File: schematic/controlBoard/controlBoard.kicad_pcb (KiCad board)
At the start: 2 copper layers, 55 x 55 mm, 40 parts, among them CON0 PINHD-1X10, IC2 DS3231/SO, IC3 LM1117?-MP, IC4 ESP12ESMD, T1 BC547, T2 BC547, Y1 12MHz

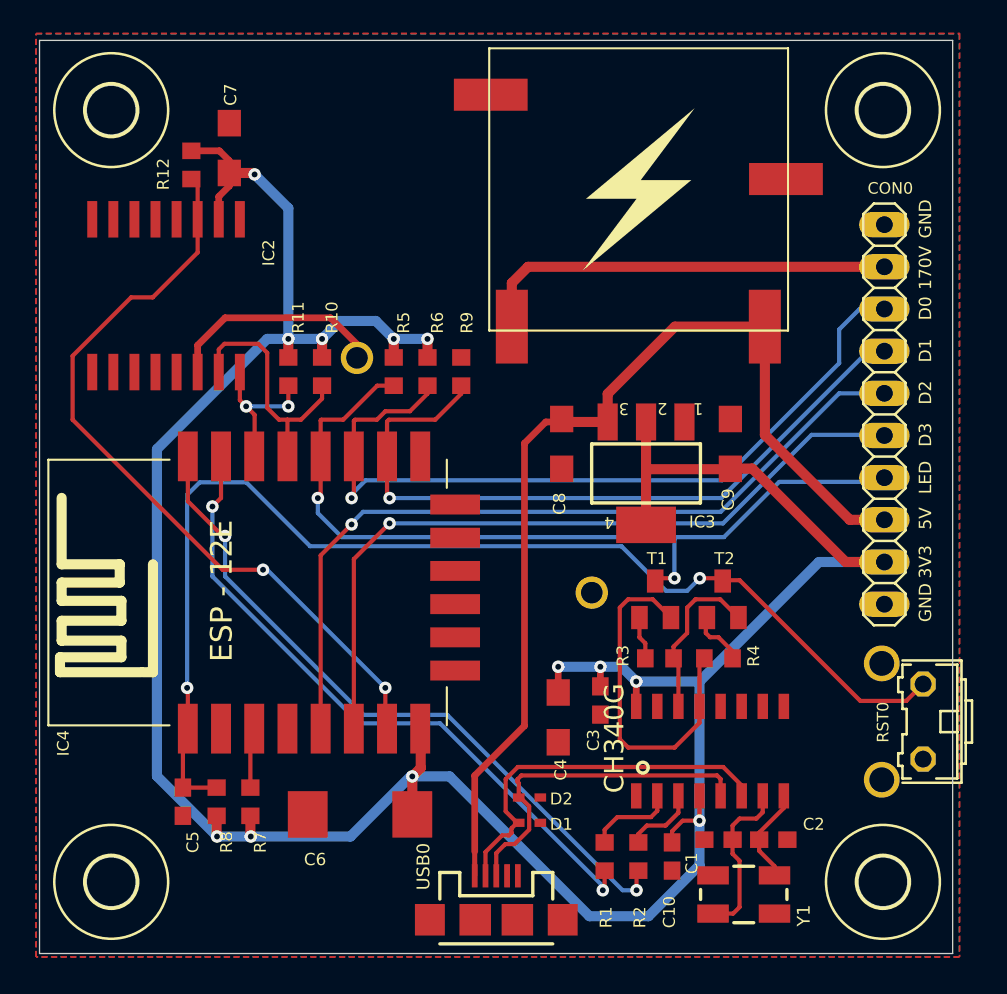
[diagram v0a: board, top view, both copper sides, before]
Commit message: Use usb type C connector and re-wire control board with KiCad components
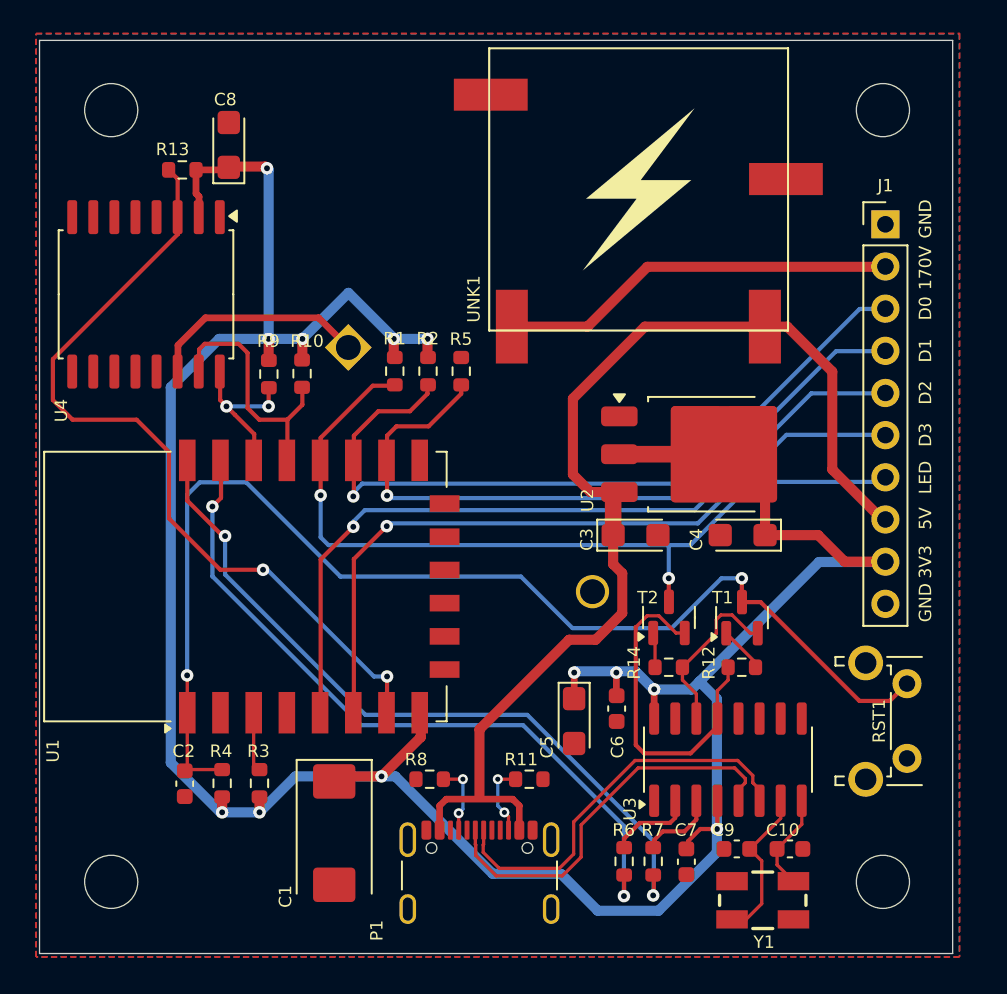
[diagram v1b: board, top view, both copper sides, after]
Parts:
- removed CON0: PINHD-1X10, controlBoard:1X10_325
- removed D1, D2: ESD321, controlBoard:SOD523_210
- removed IC2: DS3231/SO, controlBoard:SO16W
- removed IC3: LM1117?-MP, controlBoard:SOT223
- removed IC4: ESP12ESMD, controlBoard:ESP12E-SMD
- removed RST0: 31-XX, controlBoard:B3F-31XX_377
- removed U$2: CH340G, controlBoard:SOIC16
- removed USB0: USB_MICRO-B_SMT, controlBoard:USB-MICROB_513
- added J1: Conn_01x10_Pin, Connector_PinHeader_2.54mm:PinHeader_1x10_P2.54mm_Vertical, F.Cu at (171.9, 88.6)
- added P1: USB_C_Plug_USB2.0, Connector_USB:USB_C_Receptacle_GCT_USB4105-xx-A_16P_TopMnt_Horizontal, F.Cu at (147.5, 128.8)
- added R13: 4k7, Resistor_SMD:R_0603_1608Metric, F.Cu at (129.6, 85.3)
- added R14: 12k, Resistor_SMD:R_0603_1608Metric, F.Cu at (158.9, 115.3)
- added RST1: SW_Push, Button_Switch_THT:SW_Tactile_SPST_Angled_PTS645Vx31-2LFS, F.Cu at (173.3, 116.2)
- added U1: ESP-12E, RF_Module:ESP-12E, F.Cu at (133.4, 110.4)
- added U2: LM1117DT-3.3, Package_TO_SOT_SMD:TO-252-3_TabPin2, F.Cu at (161.0, 102.4)
- added U3: CH340G, Package_SO:SOIC-16_3.9x9.9mm_P1.27mm, F.Cu at (162.5, 120.8)
- added U4: DS3231M, Package_SO:SOIC-16W_7.5x10.3mm_P1.27mm, F.Cu at (127.4, 92.8)
- BT1: value BATTERY-20MM_PTH -> Battery_Cell; footprint controlBoard:BATTCOM_20MM_PTH -> Battery:BatteryHolder_MYOUNG_BS-07-A1BJ001_CR2032
- C1: value 22p -> 100u/16V; footprint controlBoard:C0603_348 -> Capacitor_Tantalum_SMD:CP_EIA-7343-31_Kemet-D
- C10: value 100n -> 22p; footprint controlBoard:C0603_348 -> Capacitor_SMD:C_0603_1608Metric
- C2: value 22p -> 470p; footprint controlBoard:C0603_348 -> Capacitor_SMD:C_0603_1608Metric
- C3: value 100n -> 10u; footprint controlBoard:C0603_348 -> Capacitor_Tantalum_SMD:CP_EIA-3216-10_Kemet-I
- C4: footprint controlBoard:SMC_A_348 -> Capacitor_Tantalum_SMD:CP_EIA-3216-10_Kemet-I
- C5: value 470p -> 10u; footprint controlBoard:C0603_348 -> Capacitor_Tantalum_SMD:CP_EIA-3216-10_Kemet-I
- C6: value 100u/16V -> 100n; footprint controlBoard:SMC_D_348 -> Capacitor_SMD:C_0603_1608Metric
- C7: value 1u -> 100n; footprint controlBoard:SMC_A_348 -> Capacitor_SMD:C_0603_1608Metric
- C8: value 10u -> 1u; footprint controlBoard:SMC_A_348 -> Capacitor_Tantalum_SMD:CP_EIA-3216-10_Kemet-I
- C9: value 10u -> 22p; footprint controlBoard:SMC_A_348 -> Capacitor_SMD:C_0603_1608Metric
- H1, H2, H3, H4: value MOUNT-HOLE3.0 -> MountingHole; footprint controlBoard:3,0_237 -> MountingHole:MountingHole_3.2mm_M3
- R1, R2: value 470 -> 12k; footprint controlBoard:R0603_348 -> Resistor_SMD:R_0603_1608Metric
- R10, R3, R4, R5: footprint controlBoard:R0603_348 -> Resistor_SMD:R_0603_1608Metric
- R11: value 4k7 -> 5k1; footprint controlBoard:R0603_348 -> Resistor_SMD:R_0603_1608Metric
- R12: value 4k7 -> 12k; footprint controlBoard:R0603_348 -> Resistor_SMD:R_0603_1608Metric
- R6, R7: value 12k -> 470; footprint controlBoard:R0603_348 -> Resistor_SMD:R_0603_1608Metric
- R8: value 12k -> 5k1; footprint controlBoard:R0603_348 -> Resistor_SMD:R_0603_1608Metric
- R9: value 12k -> 4k7; footprint controlBoard:R0603_348 -> Resistor_SMD:R_0603_1608Metric
- T1, T2: value BC547 -> BC847; footprint controlBoard:SOT23-BEC_402 -> Package_TO_SOT_SMD:SOT-23
- moved C7 51.0 mm to (160.0, 127.0)
- moved R12 44.9 mm to (163.3, 115.3), turned to 0 degrees
- moved C2 35.6 mm to (129.8, 122.3), turned to -90 degrees
- moved R2 31.9 mm to (144.4, 97.4), turned to 90 degrees
- moved R1 31.9 mm to (142.4, 97.4), turned to 90 degrees
- moved R6 31.8 mm to (156.2, 127.0), turned to -90 degrees
- moved R4 30.8 mm to (132.0, 122.2), turned to -90 degrees
- moved R11 28.5 mm to (150.5, 122.0), turned to 0 degrees
- moved C8 27.0 mm to (132.4, 83.8), turned to 90 degrees
- moved R3 25.2 mm to (134.2, 122.2), turned to -90 degrees
- moved R7 24.5 mm to (158.0, 127.0)
- moved C9 24.4 mm to (163.0, 126.2), turned to 180 degrees
- moved C5 24.1 mm to (153.2, 118.5)
- moved C1 23.1 mm to (138.8, 125.2), turned to -90 degrees
- moved C6 16.7 mm to (155.8, 117.8), turned to -90 degrees
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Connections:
- C1 pad 1: GND -> +3V3
- C1 pad 2: /XI -> GND
- C10 pad 1: +3V3 -> Net-(U3-XO)
- C2 pad 1: GND -> /RST
- C2 pad 2: /XO -> GND
- C3 pad 1: GND -> +5V
- C3 pad 2: +3V3 -> GND
- C5 pad 1: /RST -> +3V3
- R1 pad 1: Net-(U$2-TX) -> /GPIO0
- R1 pad 2: /RX -> +3V3
- R10 pad 1: +3V3 -> /SDA
- R10 pad 2: /SDA -> +3V3
- R11 pad 1: +3V3 -> Net-(P1-VCONN)
- R11 pad 2: /SCL -> GND
- R12 pad 1: +3V3 -> Net-(T2-E)
- R12 pad 2: /SQW -> Net-(T1-B)
- R2 pad 1: Net-(U$2-RX) -> /GPIO2
- R2 pad 2: /TX -> +3V3
- R3 pad 1: Net-(R3-Pad1) -> /EN
- R3 pad 2: Net-(U$2-RTS) -> +3V3
- R4 pad 1: Net-(R4-Pad1) -> /RST
- R4 pad 2: Net-(U$2-DTR) -> +3V3
- R5 pad 1: /GPIO0 -> /GPIO15
- R5 pad 2: +3V3 -> GND
- R6 pad 1: /GPIO2 -> Net-(U3-TXD)
- R6 pad 2: +3V3 -> /RX
- R7 pad 1: /EN -> Net-(U3-RXD)
- R7 pad 2: +3V3 -> /TX
- R8 pad 1: /RST -> Net-(P1-CC)
- R8 pad 2: +3V3 -> GND
- R9 pad 1: /GPIO15 -> /SCL
- R9 pad 2: GND -> +3V3
- UNK1 pad OUT: 170V -> VCC
- Y1 pad 1: /XI -> Net-(U3-XI)
- Y1 pad 3: /XO -> Net-(U3-XO)
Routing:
- net 170V: track 25.5 -> 0.00 mm
- net /D-: track 0.00 -> 24.5 mm
- net VCC: track 0.00 -> 23.9 mm
- net /D+: track 0.00 -> 23.9 mm
- net /D_N: track 22.8 -> 0.00 mm
- net Net-(U$2-DTR): track 21.3 -> 0.00 mm
- net /D_P: track 20.7 -> 0.00 mm
- net Net-(T2-E): track 0.00 -> 19.7 mm
- net Net-(T1-E): track 0.00 -> 10.2 mm
- net Net-(U$2-RTS): track 10.2 -> 0.00 mm
- net /XI: track 9.98 -> 0.00 mm
- net Net-(U3-XI): track 0.00 -> 9.47 mm
- net Net-(U3-XO): track 0.00 -> 6.61 mm
- net +5V: track 61.8 -> 68.0 mm
- net /XO: track 5.79 -> 0.00 mm
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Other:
- board text added: "Single digit nixie clock - Control board Daniel Knežević 2025"
- board text removed: "Single digit nixie clock - Control board Daniel Knežević 2024"

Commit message: Re-wire control display with KiCad components
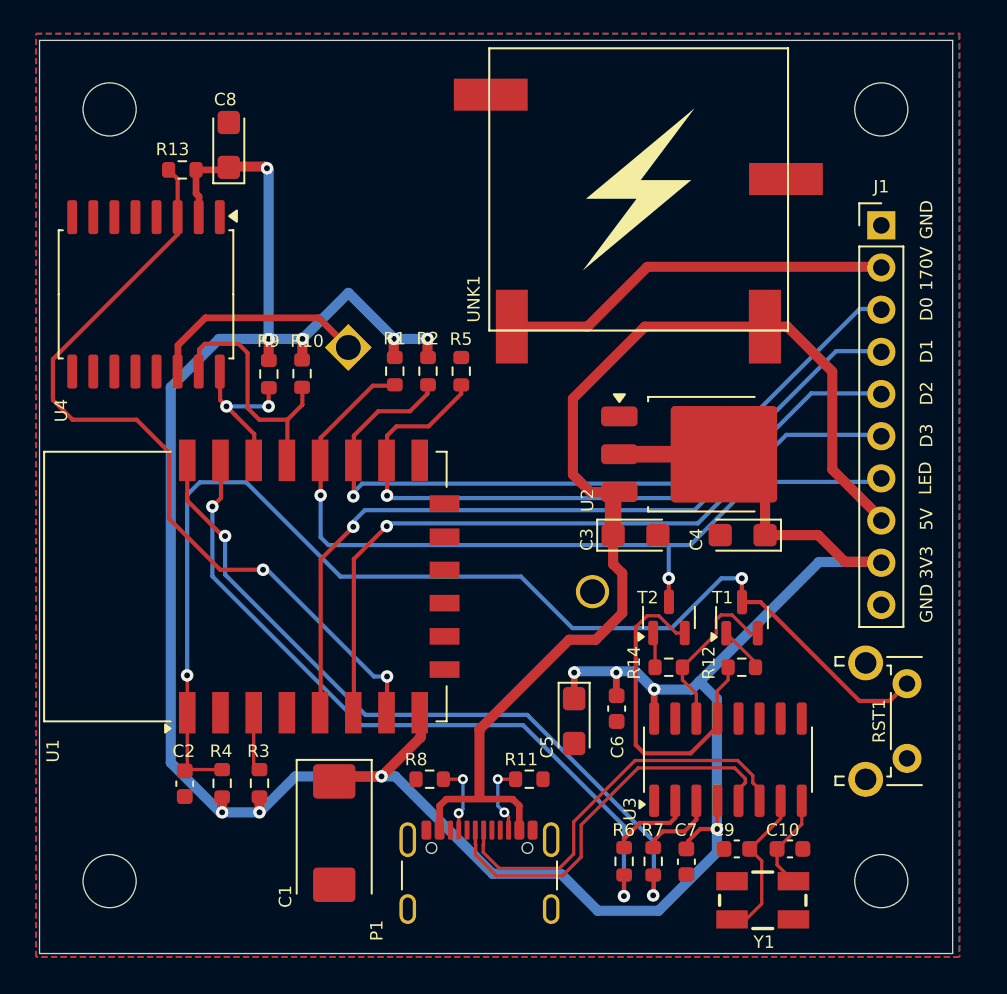
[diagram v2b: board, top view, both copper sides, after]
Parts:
- moved J1 0.25 mm to (171.7, 88.6)
- moved H2 0.11 mm to (125.2, 81.7)
- moved H3 0.11 mm to (125.2, 128.1)
- moved H1 0.11 mm to (171.7, 81.7)
- moved H4 0.11 mm to (171.7, 128.1)
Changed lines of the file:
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@@
 	(footprint "MountingHole:MountingHole_3.2mm_M3"
 		(layer "F.Cu")
-		(at 171.8011 81.7036)
+		(at 171.704 81.661)
 		(descr "Mounting Hole 3.2mm, no annular, M3")
 		(tags "mounting hole 3.2mm no annular m3")
@@
 	(footprint "MountingHole:MountingHole_3.2mm_M3"
 		(layer "F.Cu")
-		(at 125.3191 128.1856)
+		(at 125.222 128.143)
 		(descr "Mounting Hole 3.2mm, no annular, M3")
 		(tags "mounting hole 3.2mm no annular m3")
@@
 	(footprint "Connector_PinHeader_2.54mm:PinHeader_1x10_P2.54mm_Vertical"
 		(layer "F.Cu")
-		(at 171.95 88.58)
+		(at 171.704 88.646)
 		(descr "Through hole straight pin header, 1x10, 2.54mm pitch, single row")
 		(tags "Through hole pin header THT 1x10 2.54mm single row")
@@
 	(footprint "MountingHole:MountingHole_3.2mm_M3"
 		(layer "F.Cu")
-		(at 125.3191 81.7036)
+		(at 125.222 81.661)
 		(descr "Mounting Hole 3.2mm, no annular, M3")
 		(tags "mounting hole 3.2mm no annular m3")
@@
 	(footprint "MountingHole:MountingHole_3.2mm_M3"
 		(layer "F.Cu")
-		(at 171.8011 128.1856)
+		(at 171.704 128.143)
 		(descr "Mounting Hole 3.2mm, no annular, M3")
 		(tags "mounting hole 3.2mm no annular m3")
@@
 	)
 	(gr_text "170V"
-		(at 173.9211 89.8716 90)
+		(at 173.99 89.916 90)
 		(layer "F.SilkS")
 		(effects
@@
 	)
 	(gr_text "3V3"
-		(at 173.9211 107.9056 90)
+		(at 173.99 107.95 90)
 		(layer "F.SilkS")
 		(effects
@@
 	)
 	(gr_text "LED"
-		(at 173.9211 102.8256 90)
+		(at 173.9211 102.87 90)
 		(layer "F.SilkS")
 		(effects
@@
 	)
 	(gr_text "5V"
-		(at 173.9211 105.6196 90)
+		(at 173.99 105.664 90)
 		(layer "F.SilkS")
 		(effects
@@
 	)
 	(gr_text "D3"
-		(at 173.9211 100.5396 90)
+		(at 173.99 100.584 90)
 		(layer "F.SilkS")
 		(effects
@@
 	)
 	(gr_text "GND"
-		(at 173.9211 87.0776 90)
+		(at 173.99 87.122 90)
 		(layer "F.SilkS")
 		(effects
@@
 	)
 	(gr_text "D2"
-		(at 173.9211 97.9996 90)
+		(at 173.99 98.044 90)
 		(layer "F.SilkS")
 		(effects
@@
 	)
 	(gr_text "D1"
-		(at 173.9211 95.4596 90)
+		(at 173.99 95.504 90)
 		(layer "F.SilkS")
 		(effects
@@
 	)
 	(gr_text "D0"
-		(at 173.9211 92.9196 90)
+		(at 173.99 92.964 90)
 		(layer "F.SilkS")
 		(effects
@@
 	)
 	(gr_text "GND"
-		(at 173.9211 110.1916 90)
+		(at 173.99 110.236 90)
 		(layer "F.SilkS")
 		(effects

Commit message: Update control board with updated usb-c wiring
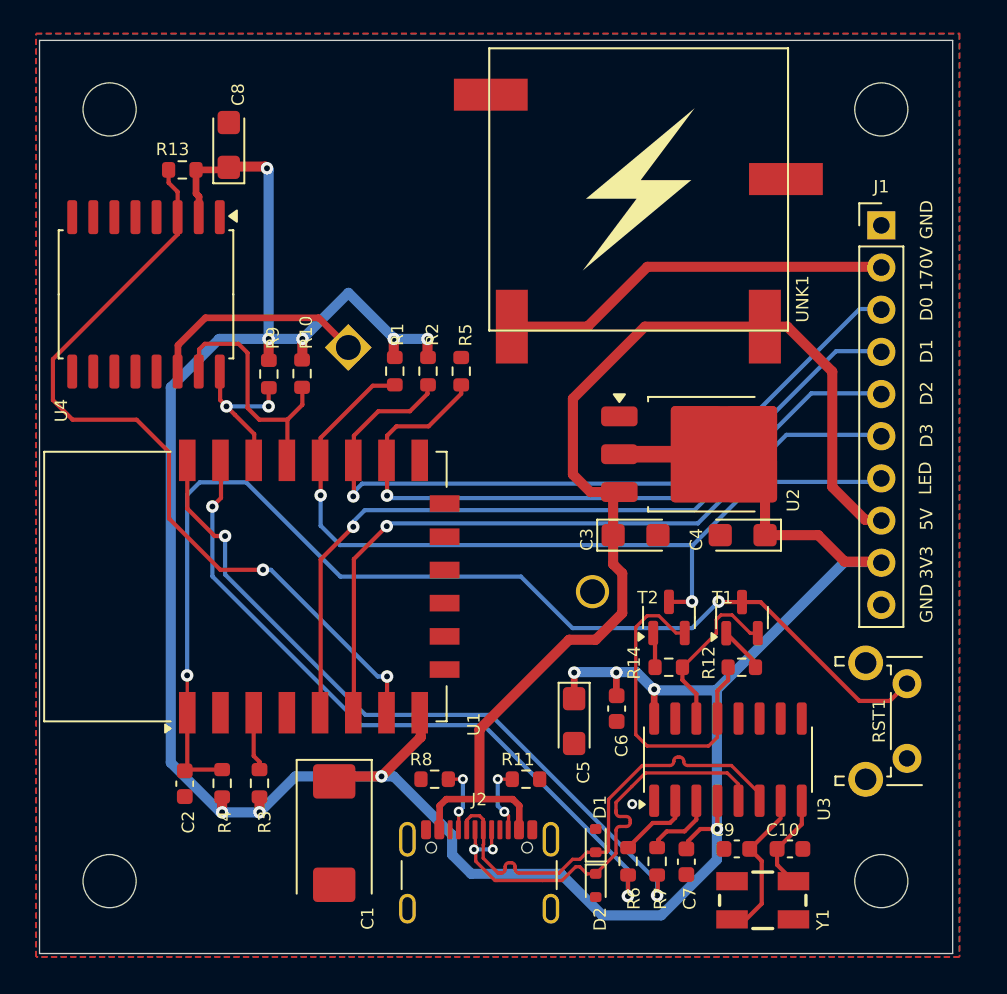
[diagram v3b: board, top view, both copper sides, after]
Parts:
- removed P1: USB_C_Plug_USB2.0, Connector_USB:USB_C_Receptacle_GCT_USB4105-xx-A_16P_TopMnt_Horizontal
- added D1: ESD321, Diode_SMD:D_SOD-523, F.Cu at (154.5, 125.7)
- added D2: ESD321, Diode_SMD:D_SOD-523, F.Cu at (154.5, 128.4)
- added J2: USB_C_Receptacle_USB2.0_14P, Connector_USB:USB_C_Receptacle_GCT_USB4105-xx-A_16P_TopMnt_Horizontal, F.Cu at (147.5, 128.7)
- moved R8 0.30 mm to (144.8, 122.0)
- moved R6 0.24 mm to (156.5, 127.0)
- moved R7 0.24 mm to (158.2, 127.0)
- moved R11 0.20 mm to (150.3, 122.0)
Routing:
- net /D+: track 23.9 -> 27.9 mm, vias 0 -> 2
- net /D-: track 24.5 -> 28.1 mm
- net /RX: track 43.6 -> 42.4 mm
- net /RST: track 71.1 -> 69.9 mm
- net /GPIO0: track 51.2 -> 52.1 mm
- net /TX: track 45.1 -> 44.2 mm
- net +5V: track 68.0 -> 68.6 mm
- net Net-(U3-TXD): track 4.99 -> 4.44 mm
- net GND: vias 0 -> 1

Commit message: Use ESP32 instead of ESP8266
- Re-route PCB to support ESP32
- Fill top plane with +3v3
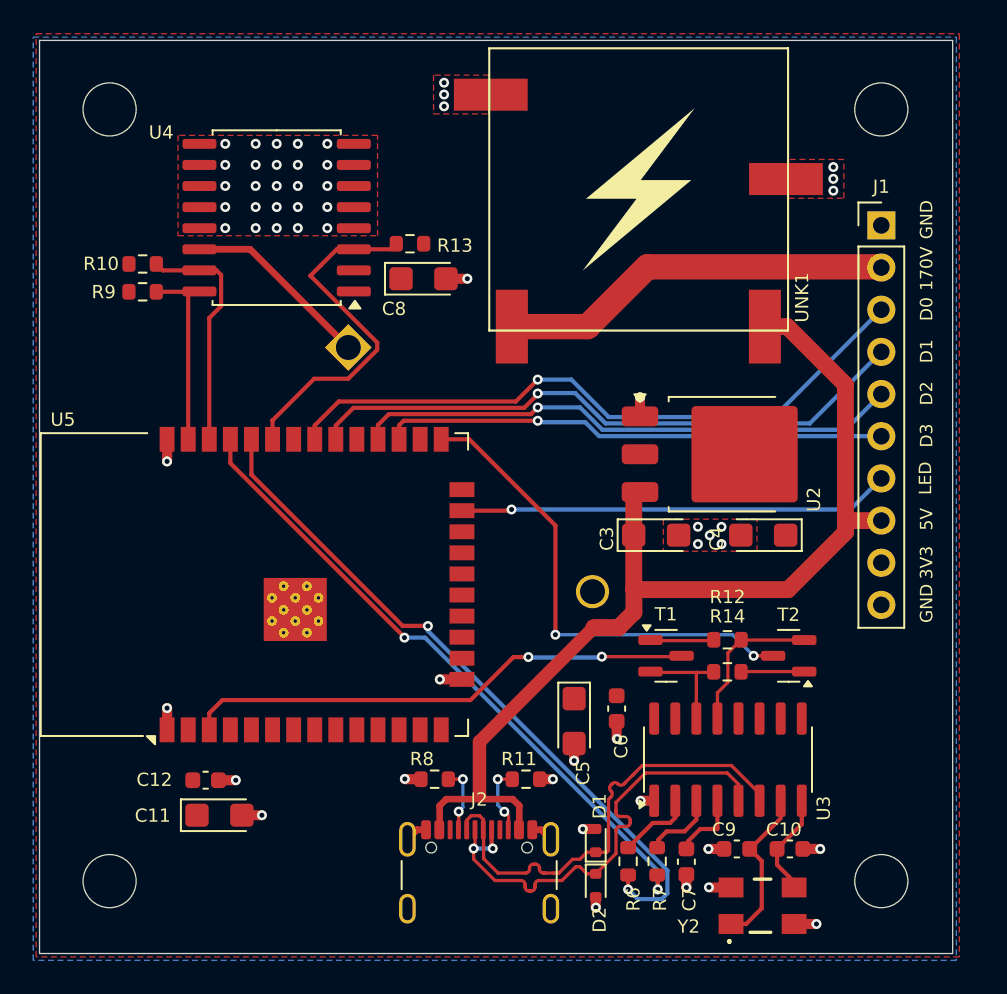
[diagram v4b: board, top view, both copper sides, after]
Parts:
- removed C1: 100u/16V, Capacitor_Tantalum_SMD:CP_EIA-7343-31_Kemet-D
- removed C2: 470p, Capacitor_SMD:C_0603_1608Metric
- removed R1, R2, R3, R4, R5: 12k, Resistor_SMD:R_0603_1608Metric
- removed RST1: SW_Push, Button_Switch_THT:SW_Tactile_SPST_Angled_PTS645Vx31-2LFS
- removed U1: ESP-12E, RF_Module:ESP-12E
- removed Y1: 12MHz, controlBoard:CRYSTAL-SMD-5X3.2-4PAD
- added C11: 10u, Capacitor_Tantalum_SMD:CP_EIA-3216-10_Kemet-I, F.Cu at (131.8, 124.2)
- added C12: 100n, Capacitor_SMD:C_0603_1608Metric, F.Cu at (131.0, 122.1)
- added U5: ESP32-WROOM-32D, RF_Module:ESP32-WROOM-32D-no-keepout, F.Cu at (136.9, 110.3)
- added Y2: 405I35D25M00000, cristal:405I35D25M00000, F.Cu at (164.6, 129.6)
- moved R13 14.4 mm to (143.3, 89.8)
- moved C8 14.2 mm to (144.1, 91.9), turned to 0 degrees
- moved R10 11.7 mm to (127.2, 91.0), turned to 180 degrees
- moved U4 9.12 mm to (135.3, 88.2), turned to 180 degrees
- moved R9 9.07 mm to (127.2, 92.6), turned to 180 degrees
- moved T2 7.57 mm to (166.1, 114.6), turned to 180 degrees
- moved T1 5.12 mm to (158.7, 114.6), turned to 0 degrees
- moved R14 3.54 mm to (162.4, 115.5), turned to 0 degrees
- moved R12 1.87 mm to (162.4, 113.6), turned to 180 degrees
- moved C4 1.24 mm to (164.6, 107.3)
- moved C3 1.24 mm to (158.1, 107.3)
- moved U2 1.24 mm to (162.2, 102.4)
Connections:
- net Net-(U3-XI) renamed /XI
- net Net-(U3-XO) renamed /XO
- J1 pad 3: /GPIO2 -> /D0
- J1 pad 4: /GPIO15 -> /D1
- J1 pad 5: /GPIO14 -> /D2
- J1 pad 6: /GPIO12 -> /D3
- J1 pad 7: /GPIO0 -> /RGBLED
- T1 pad 3: /RST -> /EN
- T2 pad 3: /GPIO0 -> /IO0
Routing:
- net +3V3: track 171.8 -> 5.14 mm, vias 12 -> 0
- net /RST: track 69.9 -> 0.00 mm, vias 2 -> 0
- net /GPIO0: track 52.1 -> 0.00 mm, vias 2 -> 0
- net /GPIO14: track 48.5 -> 0.00 mm, vias 1 -> 0
- net /GPIO2: track 46.4 -> 0.00 mm, vias 1 -> 0
- net /GPIO12: track 45.3 -> 0.00 mm, vias 1 -> 0
- net /GPIO15: track 43.3 -> 0.00 mm, vias 1 -> 0
- net /D0: track 0.00 -> 39.7 mm, vias 0 -> 1
- net /D1: track 0.00 -> 37.1 mm, vias 0 -> 1
- net /D2: track 0.00 -> 33.1 mm, vias 0 -> 1
- net /D3: track 0.00 -> 30.4 mm, vias 0 -> 1
- net /IO0: track 0.00 -> 29.2 mm, vias 0 -> 2
- net /SQW: track 49.6 -> 21.3 mm, vias 2 -> 0
- net /EN: track 3.57 -> 30.9 mm, vias 0 -> 2
- net /RGBLED: track 0.00 -> 26.1 mm, vias 0 -> 1
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- added copper zone on F.Cu, net +3V3
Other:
- board text added: "Single digit nixie clock - Control board ESP32 Daniel Knežević 2025"
- board text removed: "Single digit nixie clock - Control board Daniel Knežević 2025"
